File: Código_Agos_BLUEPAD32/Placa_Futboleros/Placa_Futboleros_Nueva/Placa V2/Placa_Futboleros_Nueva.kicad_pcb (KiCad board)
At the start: 2 copper layers, 50 x 100 mm, 16 parts, among them J1 BAT, J2 Motor_Izq_Adelante, J3 Motor_Izq_Atras, J4 Motor_Der_Adelante, J5 Motor_Der_Atras, U1 AMS1117, U2 esp32_36_pins-custom_library, U3 DRV8833, U4 DRV8833

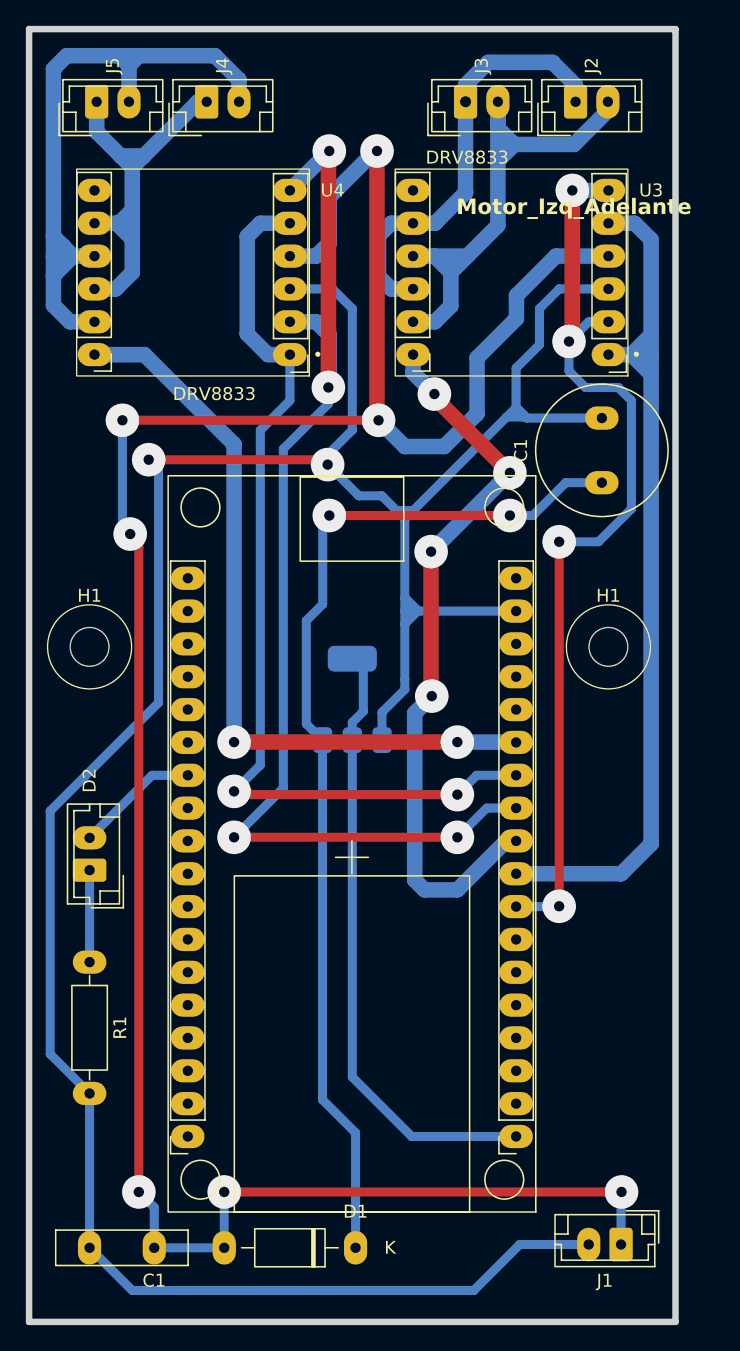
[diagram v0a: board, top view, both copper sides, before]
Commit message: Nueva versión de placa futboleros
Se diseña nuevamente la placa con las dimensiones adecuadas para el chasis
a su vez se toma el consejo del docente de agrandar el pad de disipación.
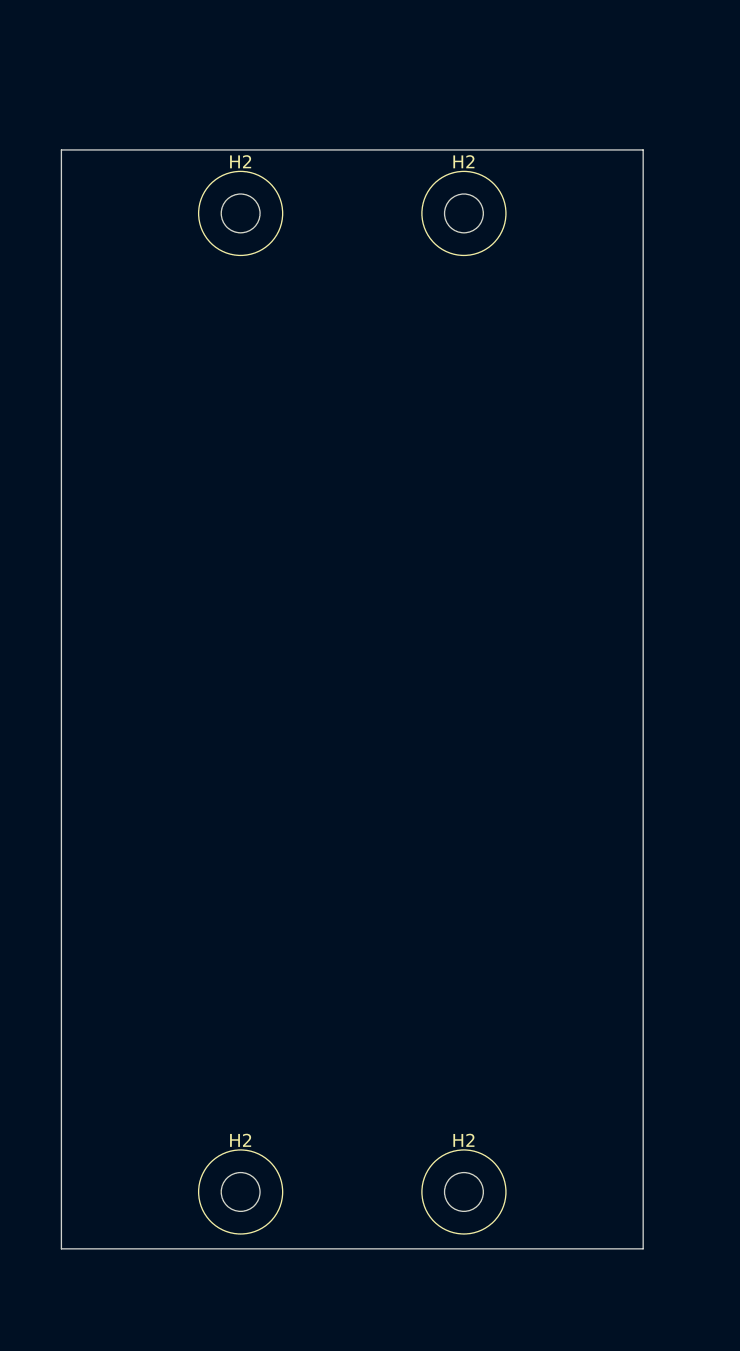
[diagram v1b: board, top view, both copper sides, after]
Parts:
- removed C1: 470uF, Capacitor_THT:C_Radial_D10.0mm_H12.5mm_P5.00mm
- removed C1: 100n, Capacitor_THT:C_Disc_D10.0mm_W2.5mm_P5.00mm
- removed D1: 1N5819, Diode_THT:D_DO-41_SOD81_P10.16mm_Horizontal
- removed D2: LED_RED, Connector_JST:JST_EH_B2B-EH-A_1x02_P2.50mm_Vertical
- removed H1 (x2): MountingHole, Futboleros:MountingHole_3mm
- removed J1: BAT, Connector_JST:JST_EH_B2B-EH-A_1x02_P2.50mm_Vertical
- removed J2: Motor_Izq_Adelante, Connector_JST:JST_EH_B2B-EH-A_1x02_P2.50mm_Vertical
- removed J3: Motor_Izq_Atras, Connector_JST:JST_EH_B2B-EH-A_1x02_P2.50mm_Vertical
- removed J4: Motor_Der_Adelante, Connector_JST:JST_EH_B2B-EH-A_1x02_P2.50mm_Vertical
- removed J5: Motor_Der_Atras, Connector_JST:JST_EH_B2B-EH-A_1x02_P2.50mm_Vertical
- removed R1: 220, Resistor_THT:R_Axial_DIN0207_L6.3mm_D2.5mm_P10.16mm_Horizontal
- removed U1: AMS1117, Package_TO_SOT_SMD:SOT-223-3_TabPin2
- removed U2: esp32_36_pins-custom_library, LibreríaProyecto:PinSocket_1x18_P2.54mm_Vertical
- removed U3, U4: DRV8833, DRV8833:DRV8833
- added H2: MountingHole, Futboleros:MountingHole_3mm, F.Cu at (165.9, 44.6)
- added H2: MountingHole, Futboleros:MountingHole_3mm, F.Cu at (165.9, 120.3)
- added H2: MountingHole, Futboleros:MountingHole_3mm, F.Cu at (183.2, 44.6)
- added H2: MountingHole, Futboleros:MountingHole_3mm, F.Cu at (183.2, 120.3)
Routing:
- net GND: track 213.6 -> 0.00 mm, vias 2 -> 0
- net VCC: track 190.7 -> 0.00 mm, vias 7 -> 0
- net IN_M2B: track 90.0 -> 0.00 mm, vias 4 -> 0
- net Net-(D1-K): track 81.1 -> 0.00 mm, vias 2 -> 0
- net IN_M2A: track 73.0 -> 0.00 mm, vias 2 -> 0
- net IN_M1B: track 72.9 -> 0.00 mm, vias 4 -> 0
- net IN_M1A: track 69.6 -> 0.00 mm
- net SLEEP_M2: track 58.5 -> 0.00 mm, vias 2 -> 0
- net SLEEP_M1: track 56.6 -> 0.00 mm, vias 4 -> 0
- net Net-(J4-Pin_2): track 51.2 -> 0.00 mm
- net +5V: track 47.3 -> 0.00 mm
- net Net-(J2-Pin_2): track 41.4 -> 0.00 mm
- net Net-(J2-Pin_1): track 33.9 -> 0.00 mm
- net Net-(J4-Pin_1): track 32.5 -> 0.00 mm
- net LED_Encendido: track 9.60 -> 0.00 mm
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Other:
- board size 50 x 100 mm -> 45 x 85 mm
